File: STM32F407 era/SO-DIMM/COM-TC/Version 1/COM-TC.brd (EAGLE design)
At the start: 127 x 165.1 mm, 170 parts, among them J1 CON1, J2 CON1, J3 SO-DIMM-CPU, J4 FTDI_DEVICE, Q4 PMV20XNE, U1 IRF9332PBF, U10 SN65HVD232D, U11 MAX9926, U12 MCP6004-E/SL, U13 MCP6004-E/SL, U14 MCP6004-E/SL, U2 5V, U3 TPS54331D, U4 3,3V, U5 MAX9926, U6 MCP6004-E/SL, U7 LoPy, U8 GTL2000, X1 057-014-1

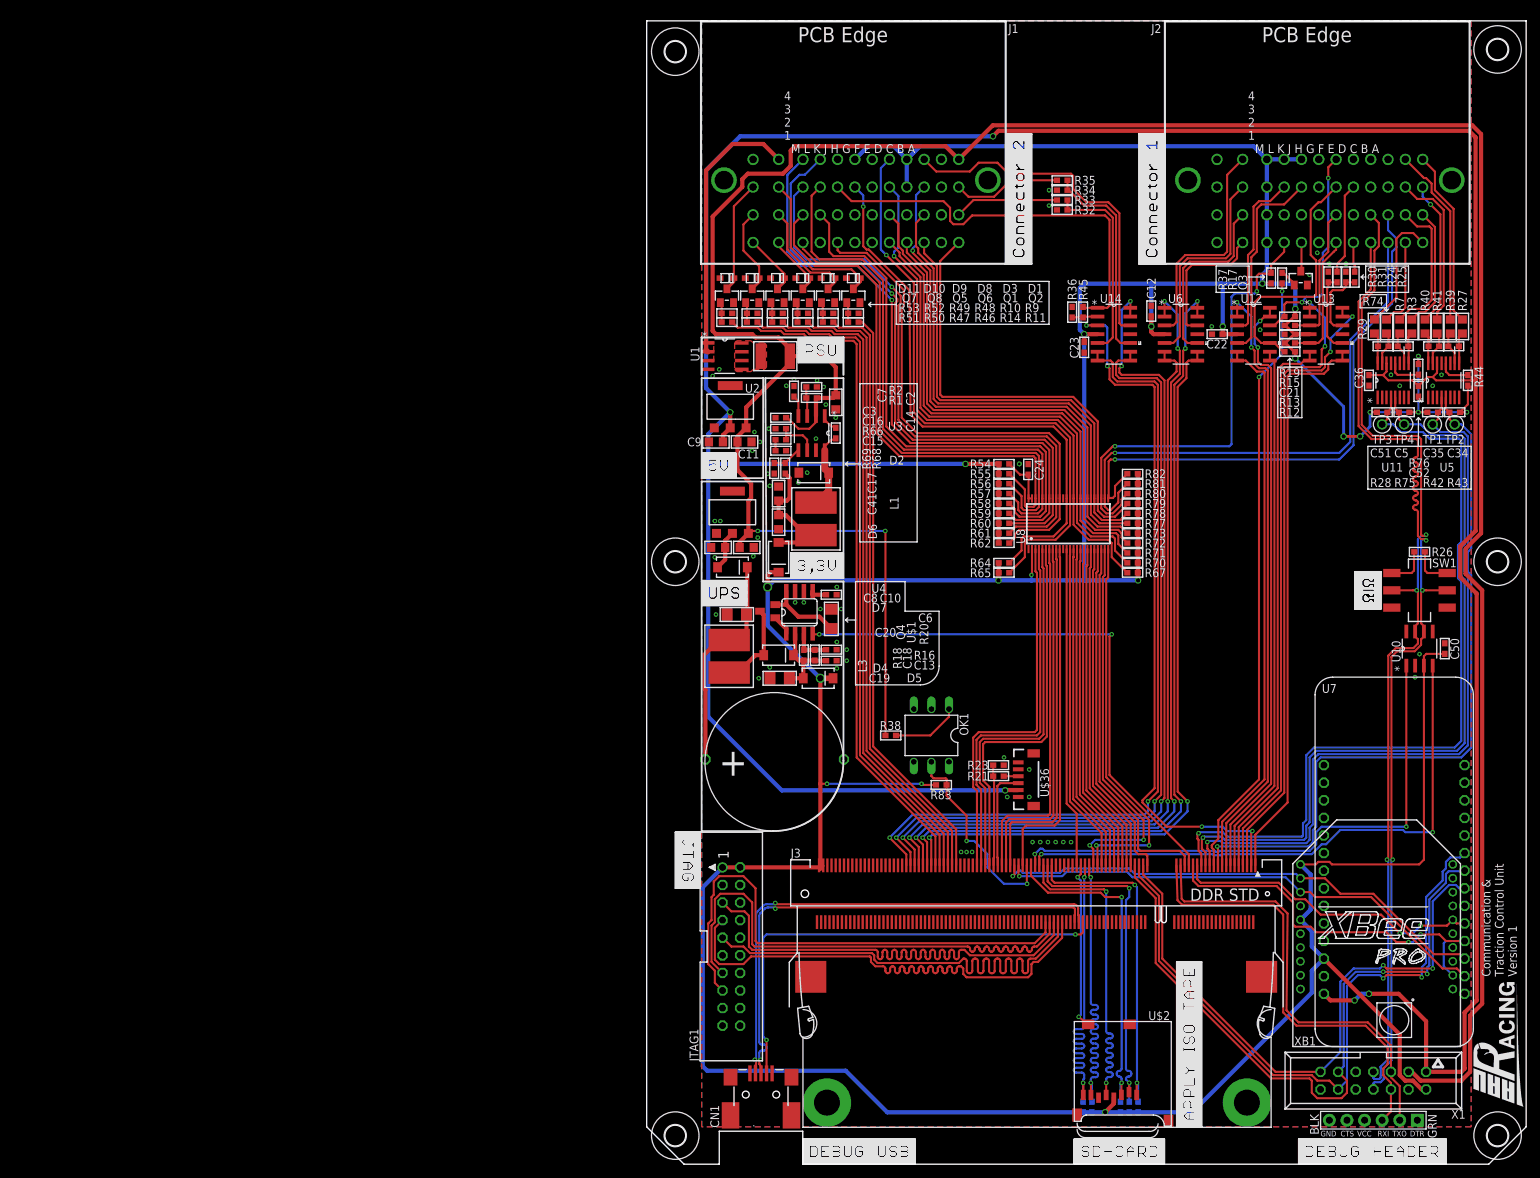
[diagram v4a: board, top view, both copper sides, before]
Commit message: last end changes on boards
Dev board
- Added 8 LED for ekstra debugging feature
- fixed Tvalue silkscreen
-

COM/TC
- fixed connections om P-channel RPP
- 12V from debug changed to include RPP and fuse

Dash
- fixed connections om P-channel RPP
- 12V from debug changed to include RPP and fuse

debug
- Added "ohm/not ohm to silkscreen
- Added BNC connectors for CAN

and much much more
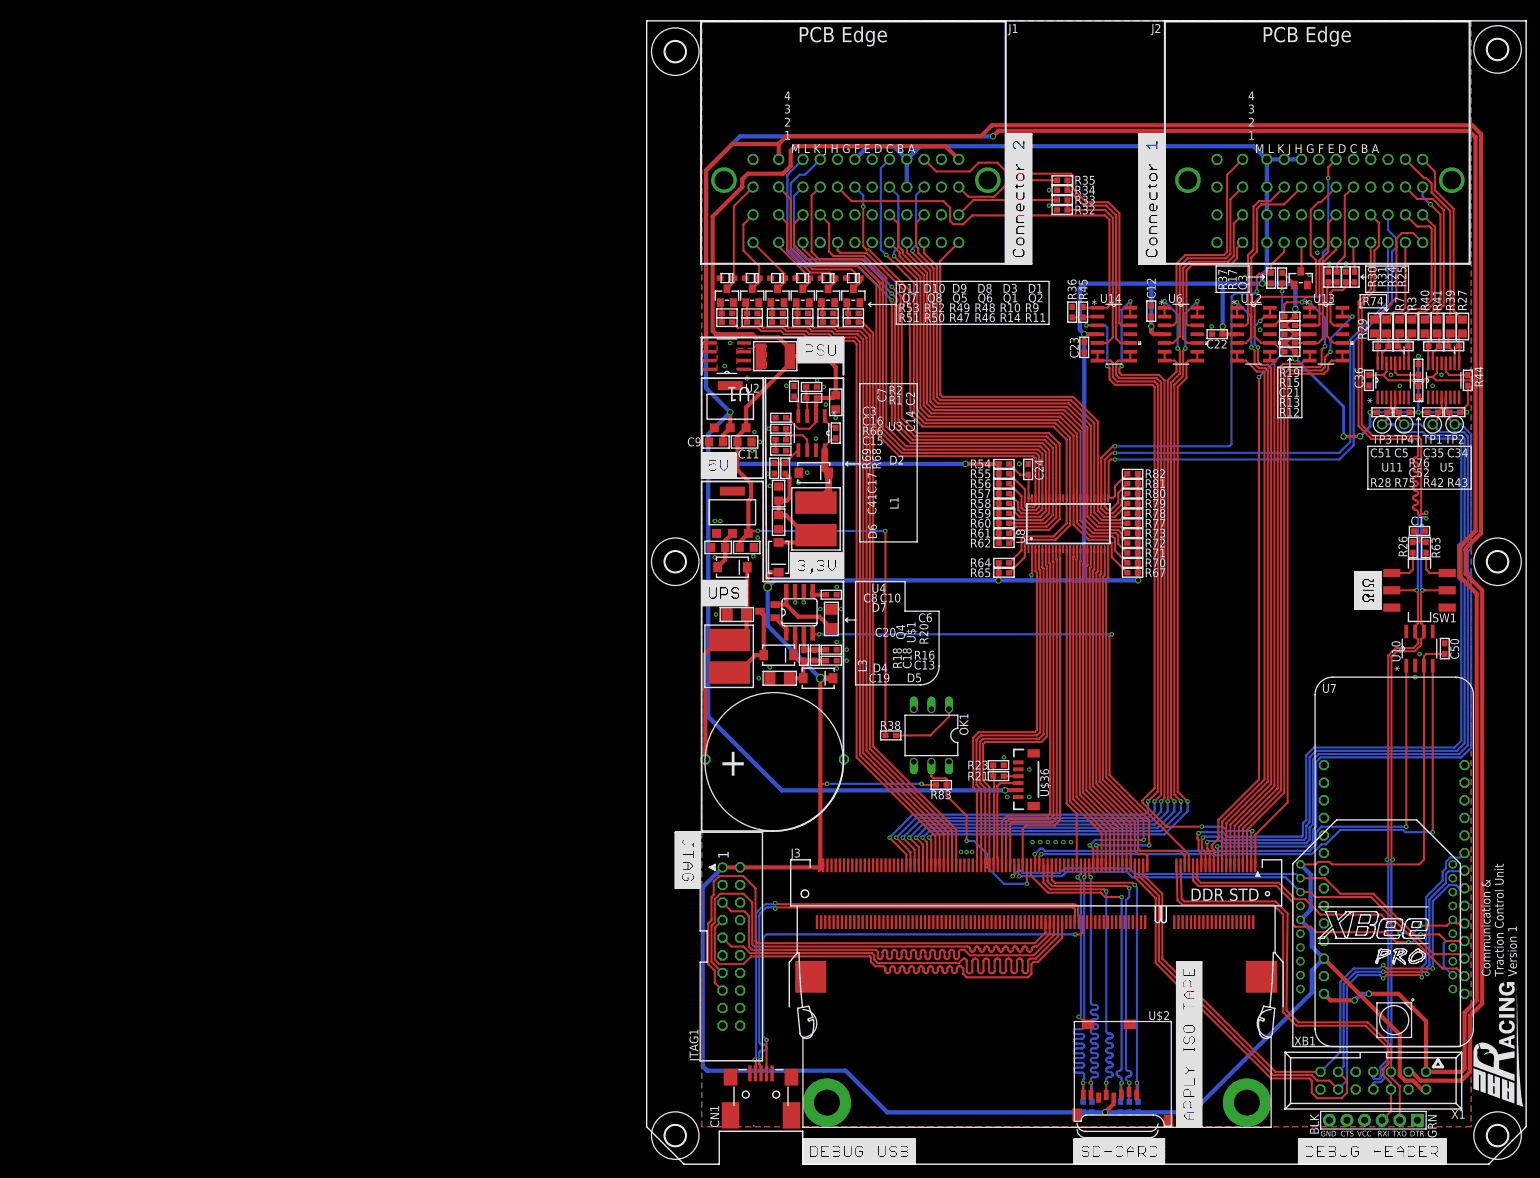
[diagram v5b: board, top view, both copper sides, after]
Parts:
- added C1: 47n, microbuilder:_0603
- added R63: 60, microbuilder:_0603
- R26: value 120 -> 60
- moved R26 1.14 mm to (110.6, 89.1), turned to 270 degrees
- moved U1 0.32 mm to (11.6, 116.7), turned to 180 degrees
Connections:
- new net N$5: R63.1, SW1.P$3
- net 12V: no longer X1.3
- net GND: now also C1.1
- net N$12: now also U1.1, U1.2, U1.3; no longer U1.5, U1.6, U1.7, U1.8
- net N$8: now also C1.2, R63.2; no longer SW1.P$3
- net VCC: now also U1.5, U1.6, U1.7, U1.8, X1.3; no longer U1.1, U1.2, U1.3
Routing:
- net VCC: track 39.3 -> 291.3 mm
- net 12V: track 403.2 -> 177.2 mm
- net N$5: track 0.00 -> 5.67 mm
- net N$8: track 6.07 -> 3.84 mm

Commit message: small error fixes
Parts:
- added C25: 100u 6v3, microbuilder:1206
- C18: value 100n -> 47p
- C19: value 220u 6v3 -> 100u 6v3
- R20: value 10m -> 35m
- R69: value 3k24 -> 2k7
- moved D4 3.05 mm to (17.6, 76.2), turned to 270 degrees
- moved Q4 1.11 mm to (17.5, 81.0)
- moved C19 0.50 mm to (19.1, 69.7)
- renumbered R16 to 50K, R18 to 70K
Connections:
- net GND: now also C25.2
- net N$28: now also C25.1
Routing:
- net N$28: track 12.9 -> 18.5 mm
- net N$36: track 12.6 -> 15.0 mm
- net N$7: track 2.94 -> 4.06 mm
- net N$27: track 11.5 -> 12.4 mm

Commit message: error corrections
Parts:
- added C26, C27: 100n, microbuilder:_0603
- added R100, R101, R98, R99: 10k 0W5, microbuilder:_0805
- added R16, R86, R87, R88, R89, R92, R93, R96, R97: 976, microbuilder:_0603
- added R18, R84, R85, R90, R91, R94, R95: 499, microbuilder:_0603
- added U9: LSM6DS3, LSM6DS3:LGA14L_DOT_INDICATOR
- R24, R30, R36: value 976 -> 499
- R33, R35: value 499 -> 976
- moved R24 30.5 mm to (70.8, 123.5)
- moved R25 28.9 mm to (73.7, 123.5)
- moved R35 27.9 mm to (80.8, 123.5), turned to 270 degrees
- moved R34 24.8 mm to (77.9, 123.5), turned to 270 degrees
- moved R30 22.4 mm to (76.5, 123.5)
- moved R33 21.8 mm to (75.1, 123.5), turned to 270 degrees
- moved R31 20.8 mm to (79.4, 123.5)
- moved R32 18.8 mm to (72.2, 123.5), turned to 270 degrees
- moved C12 8.42 mm to (73.0, 114.8)
- moved U14 7.15 mm to (67.6, 112.7)
- moved U6 7.15 mm to (77.3, 112.7)
- moved R13 7.14 mm to (92.9, 111.4)
- moved C21 7.14 mm to (92.9, 112.7)
- moved R12 7.14 mm to (92.9, 110.2)
- moved R15 7.14 mm to (92.9, 114.0)
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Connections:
- removed net CURRENT1H: J2.E1, R25.1
- removed net CURRENT1L: R24.2, R25.2, U13.12
- removed net CURRENT2H: J2.E3, R31.1
- removed net CURRENT2L: R30.2, R31.2, U13.10
- removed net GSENSL: R32.2, R33.2, U14.5
- removed net VOUT: J3.3, U14.3
- removed net VOUTB: J1.H3, R45.2, U14.1
- removed net YAWL: R34.2, R35.2, U14.10
- new net CLUTCH-POT1: R31.2, U6.12
- new net CURRENT1: J2.E1, R95.1, R97.1
- new net CURRENT2: J2.E3, R94.1, R96.1
- new net GSENSL1: R25.2, U6.5
- new net GSENSL2: R91.2, U12.5
- new net GSENSL3: R95.2, U13.12
- new net N$34: R84.2, U14.10
- new net N$35: R18.2, U7.41
- new net N$38: R45.2, U14.5
- new net N$39: R36.2, U14.3
- new net STEERING-ANGLE: J1.H3, R36.1, R86.1
- new net STEERING-ANGLE1: R24.2, U6.3
- new net STEERING-ANGLE2: R90.2, U12.3
- new net STEERING-ANGLE3: R94.2, U13.10
- new net STEERING-ANGLEB: J3.3, U14.1, U14.2
- new net YAWL1: R30.2, U6.10
- net 3.3V: now also C26.1, C27.1, U9.2, U9.3, U9.5, U9.8; no longer J1.D3, J1.D4, J1.G4, J2.H4, J2.J4, J2.K1, J2.K2, J2.K3, J2.K4, U7.3,3V
- net 5.0V: now also J1.D3, J1.D4, J1.G4, J2.H4, J2.J4, J2.K1, J2.K2, J2.K3, J2.K4
- net CLUTCH-POT: now also R85.1, R89.1; no longer U14.12
- net GEARPOSAN: now also R91.1, R93.1; no longer U12.5
- net GND: now also C26.2, C27.2, R16.2, R32.2, R33.2, R34.2, R35.2, R86.2, R87.2, R88.2, R89.2, R92.2, R93.2, R96.2, R97.2, U9.12, U9.6, U9.7; no longer R24.1, R30.1, R32.1, R34.1, R36.1
- net GSENS: now also R45.1, R87.1; no longer R33.1
- net MISO: now also U9.1
- net MOSI: now also U9.14
- net N$11: now also R100.2
- net N$13: now also R85.2, U14.12; no longer R36.2, R45.1, U14.2
- net N$15: now also R101.1
- net N$16: now also R98.2
- net N$17: now also R101.2
- net N$18: now also R100.1
- net N$19: now also R99.1
- net N$25: now also R99.2
- net N$26: now also R98.1
- net SCK: now also U9.13
- net SPEED: now also R90.1, R92.1; no longer U12.3
- net TELE_RX: now also R16.1, R18.1; no longer U7.41
- net TRAVEL1: now also R25.1, R33.1; no longer U6.5
- net TRAVEL2: now also R24.1, R32.1; no longer U6.3
- net TRAVEL3: now also R30.1, R34.1; no longer U6.10
- net TRAVEL4: now also R31.1, R35.1; no longer U6.12
- net YAW: now also R84.1, R88.1; no longer R35.1
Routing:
- net VOUT: track 102.7 -> 0.00 mm, vias 4 -> 0
- net STEERING-ANGLEB: track 0.00 -> 96.8 mm, vias 0 -> 4
- net 3.3V: track 644.2 -> 560.6 mm, vias 20 -> 22
- net VOUTB: track 59.8 -> 0.00 mm
- net STEERING-ANGLE: track 0.00 -> 45.4 mm
- net GND: track 0.00 -> 34.7 mm, vias 62 -> 64
- net MISO: track 97.3 -> 131.7 mm, vias 2 -> 4
- net SCK: track 88.4 -> 122.7 mm, vias 2 -> 4
- net MOSI: track 100.4 -> 133.7 mm
- net YAWL: track 30.0 -> 0.00 mm
- net GSENSL: track 28.3 -> 0.00 mm
- net STEERING-ANGLE3: track 0.00 -> 17.9 mm
- net N$38: track 0.00 -> 17.2 mm
- net YAW: track 15.7 -> 32.5 mm
- net N$39: track 0.00 -> 16.2 mm
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
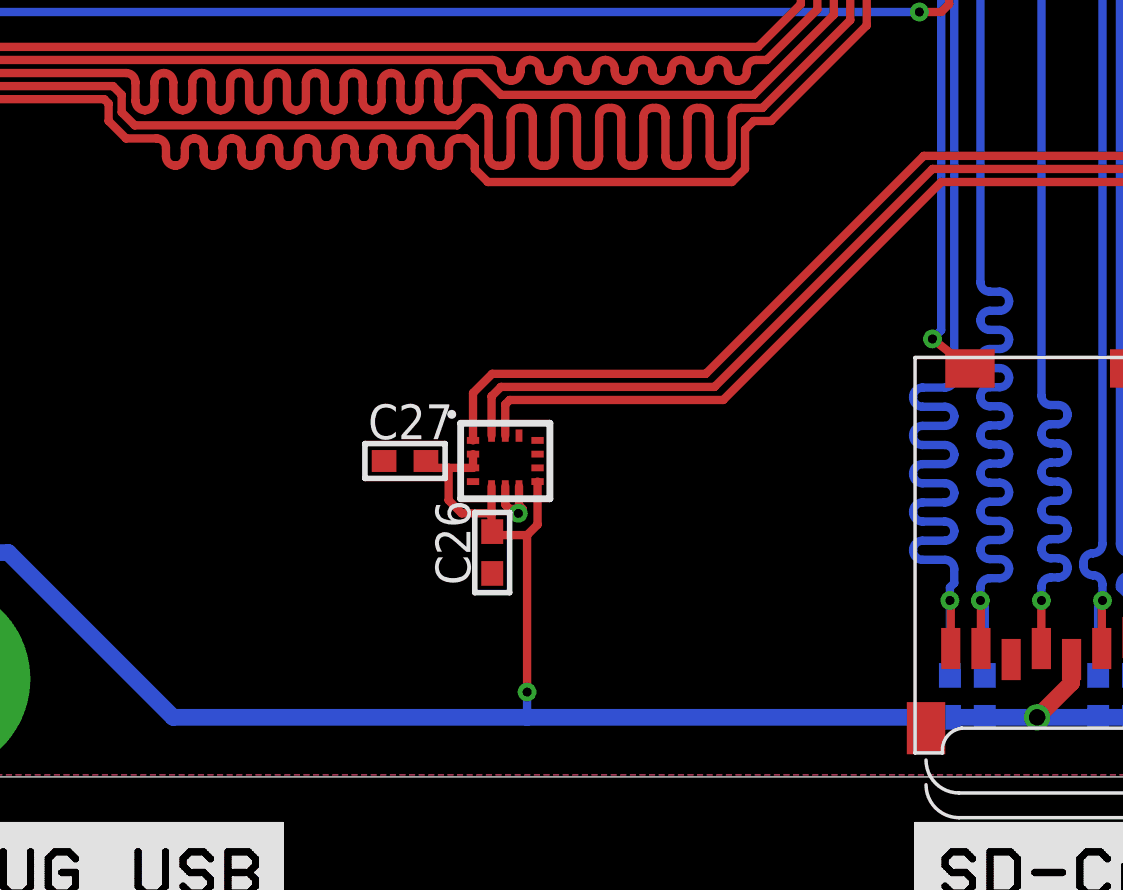
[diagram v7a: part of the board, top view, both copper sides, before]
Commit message: added accelerometer
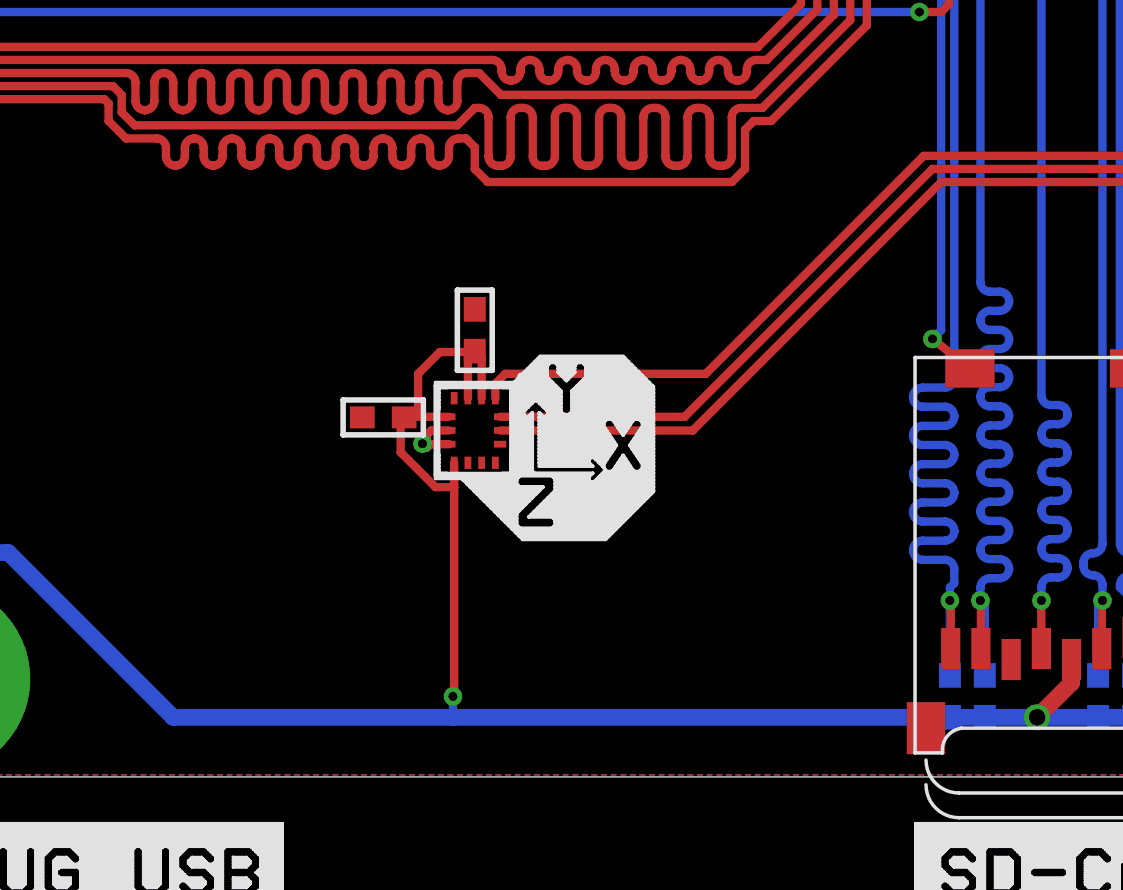
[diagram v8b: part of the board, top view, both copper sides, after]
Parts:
- moved C26 6.32 mm to (42.4, 18.4), turned to 180 degrees
- moved C27 5.40 mm to (45.7, 21.6), turned to 90 degrees
- moved U9 1.57 mm to (45.7, 17.9), turned to 270 degrees
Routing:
- net 3.3V: track 560.6 -> 565.9 mm
- net MISO: track 131.7 -> 129.5 mm
- net MOSI: track 133.7 -> 132.2 mm
- net SCK: track 122.7 -> 122.2 mm
